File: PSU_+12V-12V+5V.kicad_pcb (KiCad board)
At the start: 2 copper layers, 118.1 x 74.3 mm, 39 parts, among them Q1 BC557, Q2 BC557, Q3 BC547, Q4 BC547, U1 LM317L, U2 LM317L

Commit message: ...
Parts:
- added J1: Screw_Terminal_01x06, TerminalBlock_Phoenix:TerminalBlock_Phoenix_MKDS-1,5-6_1x06_P5.00mm_Horizontal, F.Cu at (147.3, 67.3)
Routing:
- net Net-(C13-Pad1): track 67.0 -> 102.3 mm
- net Net-(C11-Pad2): track 79.1 -> 112.6 mm
- net Net-(C14-Pad1): track 55.5 -> 75.6 mm
- net Net-(C10-Pad2): track 80.9 -> 97.8 mm

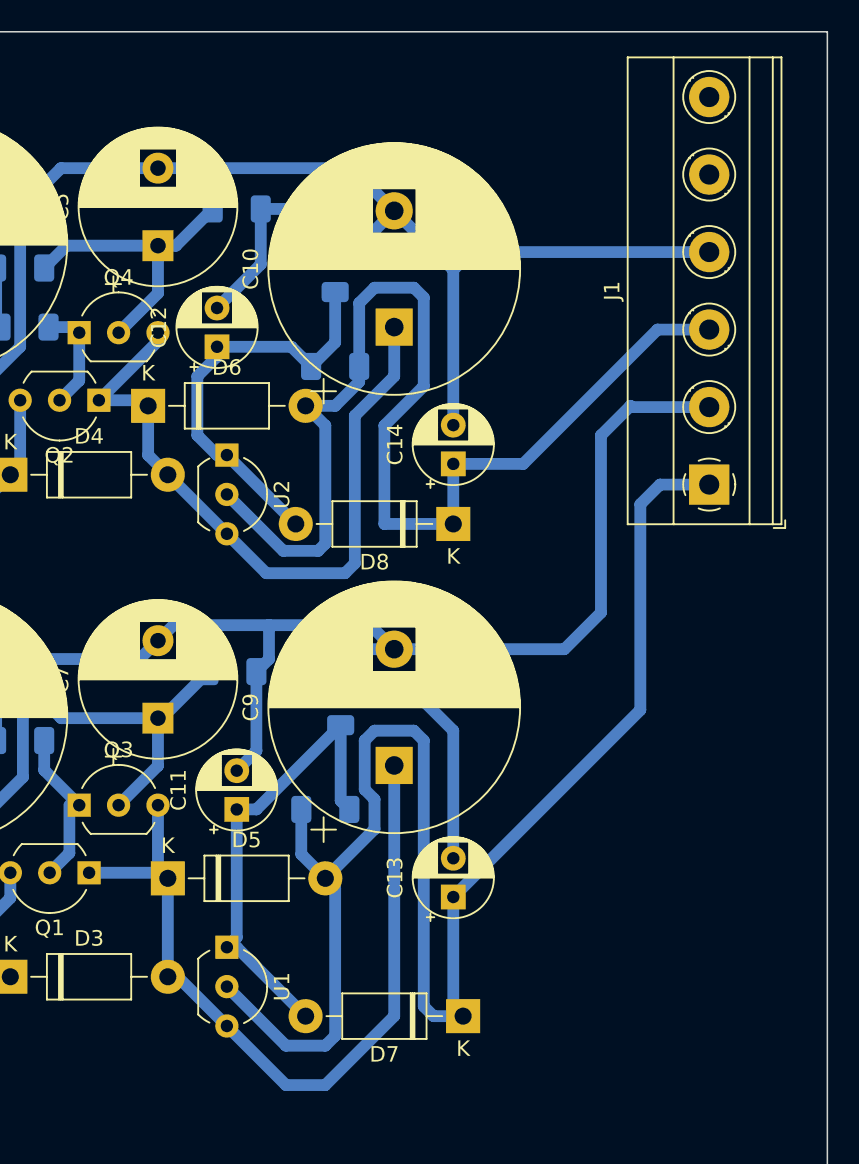
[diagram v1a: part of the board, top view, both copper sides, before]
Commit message: Herschikkingen om filled area te optimaizeren
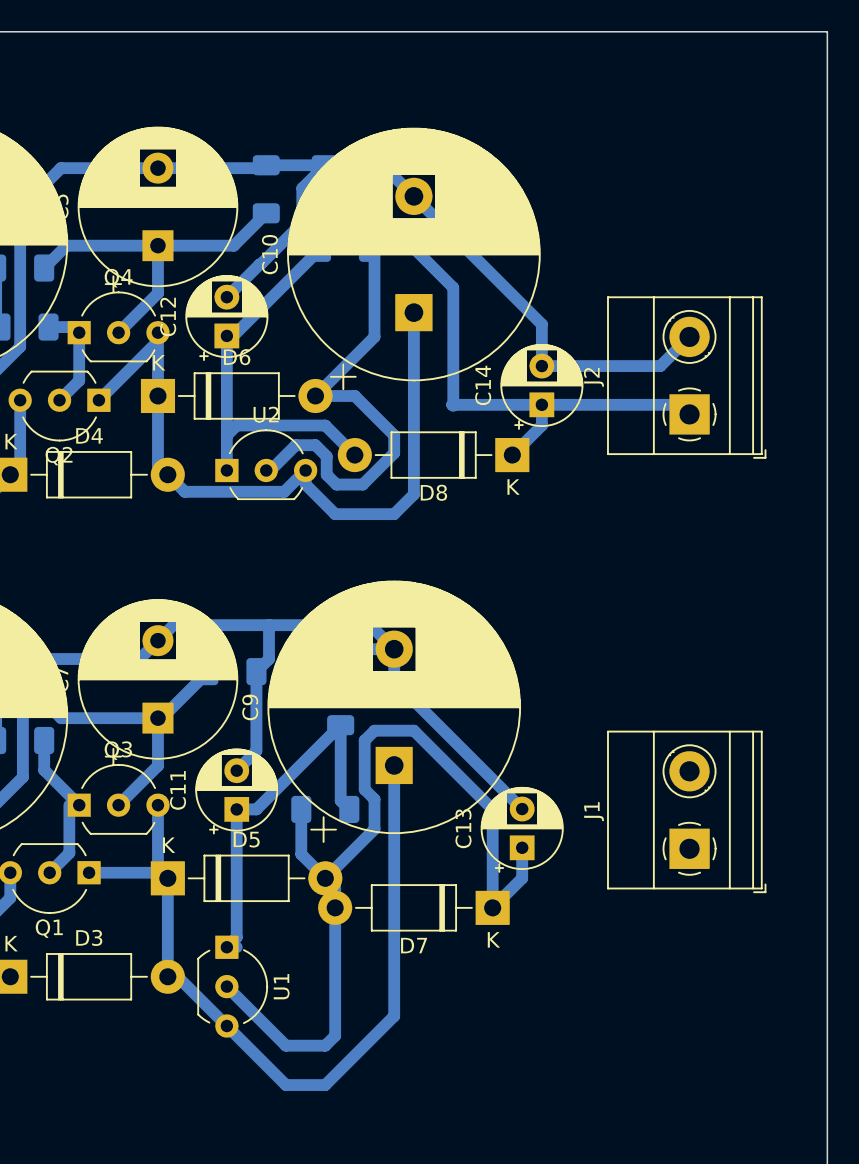
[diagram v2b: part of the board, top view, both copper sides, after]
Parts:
- added J2: Screw_Terminal_01x02, TerminalBlock_Phoenix:TerminalBlock_Phoenix_MKDS-1,5-2_1x02_P5.00mm_Horizontal, F.Cu at (146.1, 62.8)
- J1: value Screw_Terminal_01x06 -> Screw_Terminal_01x02; footprint TerminalBlock_Phoenix:TerminalBlock_Phoenix_MKDS-1,5-6_1x06_P5.00mm_Horizontal -> TerminalBlock_Phoenix:TerminalBlock_Phoenix_MKDS-1,5-2_1x02_P5.00mm_Horizontal
- moved J1 23.5 mm to (146.1, 90.8)
- moved R13 7.65 mm to (123.8, 52.1)
- moved D7 7.24 mm to (133.3, 94.6)
- moved C14 6.87 mm to (136.5, 62.2)
- moved D8 5.85 mm to (134.6, 65.4)
- moved C13 5.46 mm to (135.3, 90.7)
- moved R14 5.12 mm to (122.6, 48.3)
- moved R6 2.29 mm to (118.7, 48.3), turned to -90 degrees
- moved C10 1.58 mm to (128.3, 56.2)
- moved U2 1.00 mm to (116.2, 66.4), turned to 0 degrees
- moved C12 0.95 mm to (116.2, 57.7)
- moved D6 0.90 mm to (111.8, 61.6)
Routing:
- net Net-(C13-Pad1): track 102.3 -> 56.4 mm
- net Net-(C11-Pad2): track 112.6 -> 75.9 mm
- net Net-(C10-Pad2): track 97.8 -> 84.3 mm
- net Net-(C14-Pad1): track 75.6 -> 63.8 mm
- net Net-(C11-Pad1): track 30.7 -> 24.4 mm
- net Net-(C5-Pad1): track 19.1 -> 22.5 mm
- net Net-(C12-Pad1): track 27.0 -> 28.8 mm
- net Net-(C10-Pad1): track 45.5 -> 46.9 mm

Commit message: Some shifting
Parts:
- J1: value Screw_Terminal_01x02 -> PSU12a
- J2: value Screw_Terminal_01x02 -> PSU12b
- moved J1 9.03 mm to (141.3, 83.1)
- moved J2 8.96 mm to (141.3, 55.2)
- moved R11 6.35 mm to (122.6, 81.9), turned to 0 degrees
- moved R12 4.57 mm to (120.7, 77.8)
- moved R14 2.54 mm to (120.0, 48.3)
- moved R6 2.54 mm to (116.2, 48.3)
- moved D5 2.01 mm to (110.5, 92.1)
- moved C14 1.91 mm to (134.6, 62.2)
- moved C10 1.27 mm to (127.0, 56.2)
- moved D3 1.27 mm to (102.2, 97.8)
- moved R9 1.27 mm to (116.6, 78.1), turned to -90 degrees
- moved U1 0.73 mm to (115.6, 97.5), turned to 0 degrees
- moved D7 0.64 mm to (134.0, 94.6)
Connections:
- net Net-(C10-Pad2) renamed /0Vb
- net Net-(C11-Pad2) renamed /0Va
- net Net-(C13-Pad1) renamed /12Va
- net Net-(C14-Pad1) renamed /12Vb
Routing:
- net /0Va: track 75.9 -> 85.9 mm
- net /12Va: track 56.4 -> 62.2 mm
- net /12Vb: track 63.8 -> 58.3 mm
- net Net-(D3-Pad2): track 52.1 -> 46.8 mm
- net Net-(D7-Pad2): track 24.4 -> 27.9 mm
- net Net-(C5-Pad1): track 22.5 -> 19.9 mm
- net Net-(C7-Pad1): track 19.0 -> 20.4 mm
- net Net-(C12-Pad1): track 28.8 -> 29.6 mm
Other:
- board size 118.1 x 74.3 mm -> 95.3 x 64.8 mm

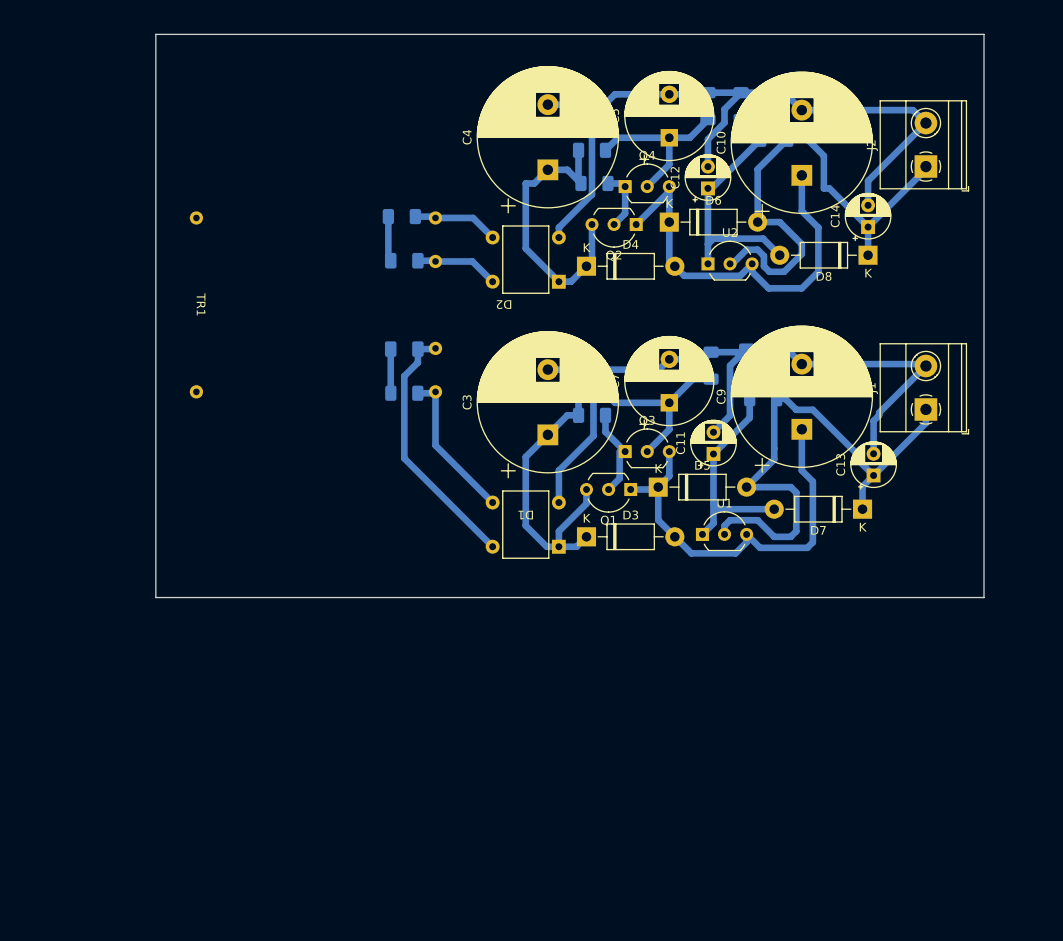
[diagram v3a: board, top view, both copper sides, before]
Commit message: Add 5V part + 230 volt connection
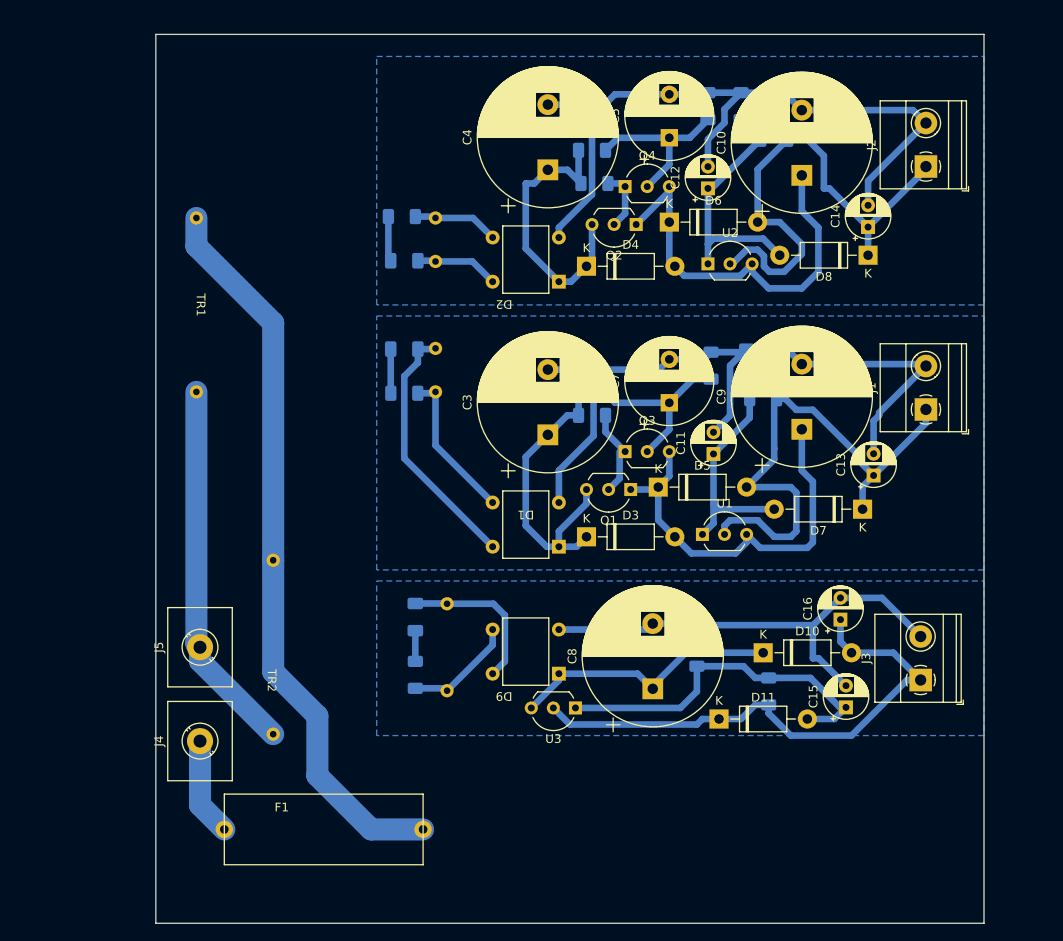
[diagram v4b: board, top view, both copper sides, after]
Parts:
- added C15: 10µ, Capacitor_THT:CP_Radial_D5.0mm_P2.50mm, F.Cu at (132.1, 117.4)
- added C16: 10µ, Capacitor_THT:CP_Radial_D5.0mm_P2.50mm, F.Cu at (131.4, 107.3)
- added C6: 0.1µ, Capacitor_SMD:C_1206_3216Metric_Pad1.33x1.80mm_HandSolder, B.Cu at (82.5, 107.0)
- added C8: 2200µ, Capacitor_THT:CP_Radial_D16.0mm_P7.50mm, F.Cu at (109.9, 115.3)
- added D10: 1N4004, Diode_THT:D_DO-41_SOD81_P10.16mm_Horizontal, F.Cu at (122.6, 111.1)
- added D11: 1N4004, Diode_THT:D_DO-41_SOD81_P10.16mm_Horizontal, F.Cu at (117.5, 118.7)
- added D9: DBL154G, MyFootPrints:DBL_4, F.Cu at (95.2, 111.1)
- added F1: Fuse, MyFootPrints:Fuse_Littelfuse-PTF15, F.Cu at (60.6, 131.4)
- added J3: PSU5, TerminalBlock_Phoenix:TerminalBlock_Phoenix_MKDS-1,5-2_1x02_P5.00mm_Horizontal, F.Cu at (140.7, 114.3)
- added J4: 230Vp, TerminalBlock_MetzConnect:TerminalBlock_MetzConnect_360271_1x01_Horizontal_ScrewM3.0_Boxed, F.Cu at (57.8, 121.3)
- added J5: 230Vn, TerminalBlock_MetzConnect:TerminalBlock_MetzConnect_360271_1x01_Horizontal_ScrewM3.0_Boxed, F.Cu at (57.8, 110.5)
- added R10: 220, Resistor_SMD:R_1206_3216Metric_Pad1.30x1.75mm_HandSolder, B.Cu at (123.2, 115.6)
- added R15: 33k, Resistor_SMD:R_1206_3216Metric_Pad1.30x1.75mm_HandSolder, B.Cu at (114.9, 111.1)
- added R8: 100, Resistor_SMD:R_1206_3216Metric_Pad1.30x1.75mm_HandSolder, B.Cu at (82.5, 113.7)
- added TR2: Gerth_304.06, MyFootPrints:304.06_1.8VA, F.Cu at (76.2, 110.5)
- added U3: LM317L, Package_TO_SOT_THT:TO-92_Inline_Wide, F.Cu at (101.0, 117.5)
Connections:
- TR1 pad 1: unconnected-(TR1-Pad1) -> /PHASE
- TR1 pad 5: unconnected-(TR1-Pad5) -> /NULL
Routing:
- net /PHASE: track 0.00 -> 84.6 mm
- net /5Vc: track 0.00 -> 62.2 mm
- net /0Vc: track 0.00 -> 55.6 mm
- net /NULL: track 0.00 -> 43.0 mm
- net Net-(C15-Pad1): track 0.00 -> 41.8 mm
- net Net-(C8-Pad1): track 0.00 -> 31.4 mm
- net Net-(C6-Pad1): track 0.00 -> 18.2 mm
- net Net-(D9-Pad3): track 0.00 -> 13.0 mm
- net /MainP: track 0.00 -> 11.3 mm
- net Net-(C6-Pad2): track 0.00 -> 3.53 mm
- added copper zone on B.Cu, net /0Va
- added copper zone on B.Cu, net /0Vc
- added copper zone on B.Cu, net /12Vb
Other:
- board size 95.3 x 64.8 mm -> 95.3 x 102.2 mm

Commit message: ...
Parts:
- removed J5: 230Vn, TerminalBlock_MetzConnect:TerminalBlock_MetzConnect_360271_1x01_Horizontal_ScrewM3.0_Boxed
- added H1: MountingHole, MountingHole:MountingHole_3.2mm_M3, F.Cu at (143.5, 137.8)
- added H2: MountingHole, MountingHole:MountingHole_3.2mm_M3, F.Cu at (55.2, 43.8)
- added H3: MountingHole, MountingHole:MountingHole_3.2mm_M3, F.Cu at (55.2, 137.8)
- added H4: MountingHole, MountingHole:MountingHole_3.2mm_M3, F.Cu at (143.5, 43.8)
- J4: value 230Vp -> 230V; footprint TerminalBlock_MetzConnect:TerminalBlock_MetzConnect_360271_1x01_Horizontal_ScrewM3.0_Boxed -> TerminalBlock_Phoenix:TerminalBlock_Phoenix_MKDS-1,5-3_1x03_P5.00mm_Horizontal
- moved J4 8.23 mm to (56.8, 113.1), turned to -90 degrees
- moved C15 7.26 mm to (134.0, 124.4)
- moved C16 7.26 mm to (133.3, 114.3)
- moved D9 7.26 mm to (97.2, 118.1)
- moved R10 7.26 mm to (125.1, 122.6)
- moved R15 7.26 mm to (116.8, 118.1)
- moved U3 7.26 mm to (102.9, 124.5)
- moved D10 7.26 mm to (124.5, 118.1)
- moved C8 7.26 mm to (111.8, 122.3)
- moved D11 7.26 mm to (119.4, 125.8)
- moved J3 7.26 mm to (142.6, 121.3)
- moved C13 3.31 mm to (136.2, 93.9)
- moved C3 3.31 mm to (98.7, 89.2)
- moved Q1 3.31 mm to (108.3, 95.5)
- moved R3 3.31 mm to (103.8, 87.0)
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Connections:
- J4 pad 1: /MainP -> /NULL
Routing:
- net Net-(C6-Pad1): track 18.2 -> 31.6 mm
- net Net-(D1-Pad3): track 17.6 -> 23.4 mm
- net Net-(C1-Pad2): track 29.6 -> 34.1 mm
- net Net-(C2-Pad2): track 9.60 -> 13.7 mm
- net Net-(D2-Pad3): track 9.89 -> 13.8 mm
- net /NULL: track 43.0 -> 45.4 mm
- net Net-(D9-Pad3): track 13.0 -> 10.9 mm
- net /MainP: track 11.3 -> 9.88 mm
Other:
- board size 95.3 x 102.2 mm -> 97.2 x 102.2 mm

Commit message: Changed footprint of LM317L
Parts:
- U1, U2, U3: footprint Package_TO_SOT_THT:TO-92_Inline_Wide -> MyFootPrints:LM317L_TO92

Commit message: Aanpassing ijkweerstand 5V
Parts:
- added R16: 560, Resistor_SMD:R_1206_3216Metric_Pad1.30x1.75mm_HandSolder, B.Cu at (120.7, 121.3)
- R15: value 33k -> 100
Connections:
- R15 pad 2: Net-(C15-Pad1) -> Net-(R15-Pad2)
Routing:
- net Net-(R15-Pad2): track 0.00 -> 2.92 mm
- net Net-(C15-Pad1): track 41.8 -> 39.2 mm
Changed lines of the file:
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@@
   (net 30 "/5Vc")
   (net 31 "unconnected-(J4-Pad2)")
+  (net 32 "Net-(R15-Pad2)")
   (footprint "Diode_THT:D_DO-41_SOD81_P10.16mm_Horizontal" (layer "F.Cu")
     (at 134.9375 97.79 180)
@@
       (effects (font (size 1 1) (thickness 0.15)) (justify mirror))
     )
-    (fp_text value "33k" (at 0 -1.82 90) (layer "B.Fab")
+    (fp_text value "100" (at 0 -1.82 90) (layer "B.Fab")
       (effects (font (size 1 1) (thickness 0.15)) (justify mirror))
     )
@@
       (net 29 "/0Vc") (pintype "passive"))
     (pad "2" smd roundrect (at 1.55 0 270) (size 1.3 1.75) (layers "B.Cu" "B.Paste" "B.Mask") (roundrect_rratio 0.192308)
-      (net 24 "Net-(C15-Pad1)") (pintype "passive"))
+      (net 32 "Net-(R15-Pad2)") (pintype "passive"))
     (model "${KICAD6_3DMODEL_DIR}/Resistor_SMD.3dshapes/R_1206_3216Metric.wrl"
       (offset (xyz 0 0 0))
@@
     )
   )
+  (footprint "Resistor_SMD:R_1206_3216Metric_Pad1.30x1.75mm_HandSolder" (layer "B.Cu")
+    (at 120.65 121.285)
+    (descr "Resistor SMD 1206 (3216 Metric), square (rectangular) end terminal, IPC_7351 nominal with elongated pad for handsoldering. (Body size source: IPC-SM-782 page 72, https://www.pcb-3d.com/wordpress/wp-content/uploads/ipc-sm-782a_amendment_1_and_2.pdf), generated with kicad-footprint-generator")
+    (tags "resistor handsolder")
+    (property "Sheetfile" "PSU_+12V-12V+5V.kicad_sch")
+    (property "Sheetname" "")
+    (attr smd)
+    (fp_text reference "R16" (at 0 1.82) (layer "B.SilkS")
+      (effects (font (size 1 1) (thickness 0.15)) (justify mirror))
+    )
+    (fp_text value "560" (at 0 -1.82) (layer "B.Fab")
+      (effects (font (size 1 1) (thickness 0.15)) (justify mirror))
+    )
+    (fp_text user "${REFERENCE}" (at 0 0) (layer "B.Fab")
+      (effects (font (size 0.8 0.8) (thickness 0.12)) (justify mirror))
+    )
+    (fp_line (start -0.727064 0.91) (end 0.727064 0.91) (layer "B.SilkS") (width 0.12))
+    (fp_line (start -0.727064 -0.91) (end 0.727064 -0.91) (layer "B.SilkS") (width 0.12))
+    (fp_line (start 2.45 1.12) (end 2.45 -1.12) (layer "B.CrtYd") (width 0.05))
+    (fp_line (start -2.45 1.12) (end 2.45 1.12) (layer "B.CrtYd") (width 0.05))
+    (fp_line (start -2.45 -1.12) (end -2.45 1.12) (layer "B.CrtYd") (width 0.05))
+    (fp_line (start 2.45 -1.12) (end -2.45 -1.12) (layer "B.CrtYd") (width 0.05))
+    (fp_line (start -1.6 -0.8) (end -1.6 0.8) (layer "B.Fab") (width 0.1))
+    (fp_line (start 1.6 -0.8) (end -1.6 -0.8) (layer "B.Fab") (width 0.1))
+    (fp_line (start 1.6 0.8) (end 1.6 -0.8) (layer "B.Fab") (width 0.1))
+    (fp_line (start -1.6 0.8) (end 1.6 0.8) (layer "B.Fab") (width 0.1))
+    (pad "1" smd roundrect (at -1.55 0) (size 1.3 1.75) (layers "B.Cu" "B.Paste" "B.Mask") (roundrect_rratio 0.192308)
+      (net 32 "Net-(R15-Pad2)") (pintype "passive"))
+    (pad "2" smd roundrect (at 1.55 0) (size 1.3 1.75) (layers "B.Cu" "B.Paste" "B.Mask") (roundrect_rratio 0.192308)
+      (net 24 "Net-(C15-Pad1)") (pintype "passive"))
+    (model "${KICAD6_3DMODEL_DIR}/Resistor_SMD.3dshapes/R_1206_3216Metric.wrl"
+      (offset (xyz 0 0 0))
+      (scale (xyz 1 1 1))
+      (rotate (xyz 0 0 0))
+    )
+  )
   (footprint "Capacitor_SMD:C_1206_3216Metric_Pad1.33x1.80mm_HandSolder" (layer "B.Cu")
     (at 81.28 66.04)
@@
   (segment (start 121.6025 84.735) (end 121.9575 85.09) (width 0.762) (layer "B.Cu") (net 23))
   (segment (start 117.7925 99.42) (end 116.5225 100.69) (width 0.762) (layer "B.Cu") (net 23))
-  (segment (start 122.2 119.684887) (end 123.545 121.029887) (width 0.762) (layer "B.Cu") (net 24))
   (segment (start 133.31 124.444887) (end 133.35 124.444887) (width 0.762) (layer "B.Cu") (net 24))
-  (segment (start 123.545 121.029887) (end 125.095 121.029887) (width 0.762) (layer "B.Cu") (net 24))
+  (segment (start 125.095 121.029887) (end 122.455113 121.029887) (width 0.762) (layer "B.Cu") (net 24))
+  (segment (start 122.2 121.64) (end 122.2 121.285) (width 0.762) (layer "B.Cu") (net 24))
+  (segment (start 120.65 123.19) (end 122.2 121.64) (width 0.762) (layer "B.Cu") (net 24))
+  (segment (start 114.910113 124.484887) (end 116.205 123.19) (width 0.762) (layer "B.Cu") (net 24))
+  (segment (start 116.205 123.19) (end 120.65 123.19) (width 0.762) (layer "B.Cu") (net 24))
   (segment (start 125.095 121.029887) (end 129.895 121.029887) (width 0.762) (layer "B.Cu") (net 24))
-  (segment (start 116.84 122.579887) (end 116.84 119.684887) (width 0.762) (layer "B.Cu") (net 24))
-  (segment (start 102.87 124.484887) (end 114.935 124.484887) (width 0.762) (layer "B.Cu") (net 24))
-  (segment (start 114.935 124.484887) (end 116.84 122.579887) (width 0.762) (layer "B.Cu") (net 24))
   (segment (start 132.650113 125.754887) (end 133.985 124.42) (width 0.762) (layer "B.Cu") (net 24))
-  (segment (start 116.84 119.684887) (end 122.2 119.684887) (width 0.762) (layer "B.Cu") (net 24))
+  (segment (start 102.87 124.484887) (end 114.910113 124.484887) (width 0.762) (layer "B.Cu") (net 24))
   (segment (start 129.54 125.754887) (end 132.650113 125.754887) (width 0.762) (layer "B.Cu") (net 24))
   (segment (start 129.895 121.029887) (end 133.285113 124.42) (width 0.762) (layer "B.Cu") (net 24))
   (segment (start 133.285113 124.42) (end 133.985 124.42) (width 0.762) (layer "B.Cu") (net 24))
+  (segment (start 122.455113 121.029887) (end 122.2 121.285) (width 0.762) (layer "B.Cu") (net 24))
   (segment (start 86.2 115.49) (end 93.319887 115.49) (width 0.762) (layer "B.Cu") (net 25))
   (segment (start 85.925 115.215) (end 86.2 115.49) (width 0.762) (layer "B.Cu") (net 25))
@@
   (segment (start 100.33 124.484887) (end 102.235 126.389887) (width 0.762) (layer "B.Cu") (net 30))
   (segment (start 127.635 127.659887) (end 134.62 127.659887) (width 0.762) (layer "B.Cu") (net 30))
+  (segment (start 117.499887 119.684887) (end 119.1 121.285) (width 0.762) (layer "B.Cu") (net 32))
+  (segment (start 116.84 119.684887) (end 117.499887 119.684887) (width 0.762) (layer "B.Cu") (net 32))
   (zone (net 29) (net_name "/0Vc") (layer "B.Cu") (hatch edge 0.508)
     (connect_pads (clearance 0.508))
